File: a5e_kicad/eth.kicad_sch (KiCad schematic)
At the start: 54 parts, among them J9 RJ45_RB1-125B8G1A, U10 KSZ9031RNXCA, Y3 25MHz

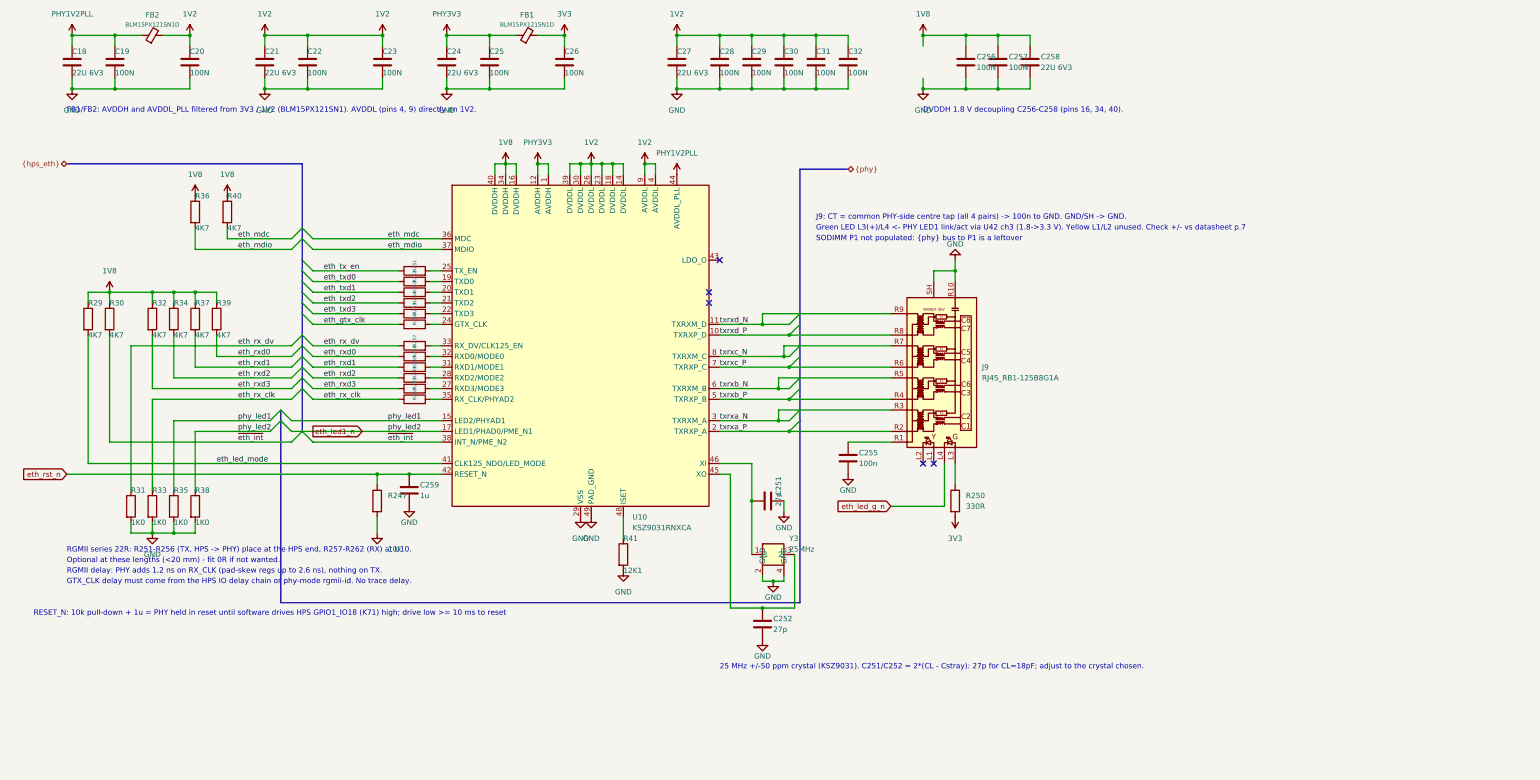
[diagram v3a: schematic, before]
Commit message: Ethernet PHY: KSZ9031RNX -> RTL8211FDI-CG (JLC stock, configured over MDIO)
The KSZ9031 had 16 orderable at JLC. The RTL8211FDI-CG (C692886) has 8.5k,
an internal 1.0 V LDO and only two straps.

- New symbol agilex_5_lib:RTL8211FDI-CG (QFN-40 5x5). Pins sit where the KSZ
  pins of the same function were, so the RGMII series resistors, MDI, crystal
  and RSET wiring are unchanged. The netlist was checked pin by pin.
- Straps: CFG_LDO = 10 (1.8 V I/O LDO) via R35 4K7 down on LED1 and new R268
  4K7 up on LED2. Everything else uses internal defaults (address 1). KSZ
  straps R29, R31-R34 and R37-R39 are DNP.
- Supplies: DVDD33 3V3, AVDD33 via FB1, LDO_OUT -> PHY1V0 (AVDD10/DVDD10,
  old 1V2 caps), DVDD_RG -> PHY_RG (caps only). FB2/C18/C19 DNP.
- PHYRSTB is a 3.3 V input: U42 ch3 now level-shifts eth_rst_n (1.8 V) to
  phy_rst_n. LED2 drives the J9 green LED directly.
- R36 MDIO pull-up 1K5, R41 RSET 2K49 1%.
- Notes on the sheet and ETH_PHY_REVIEW.md updated.
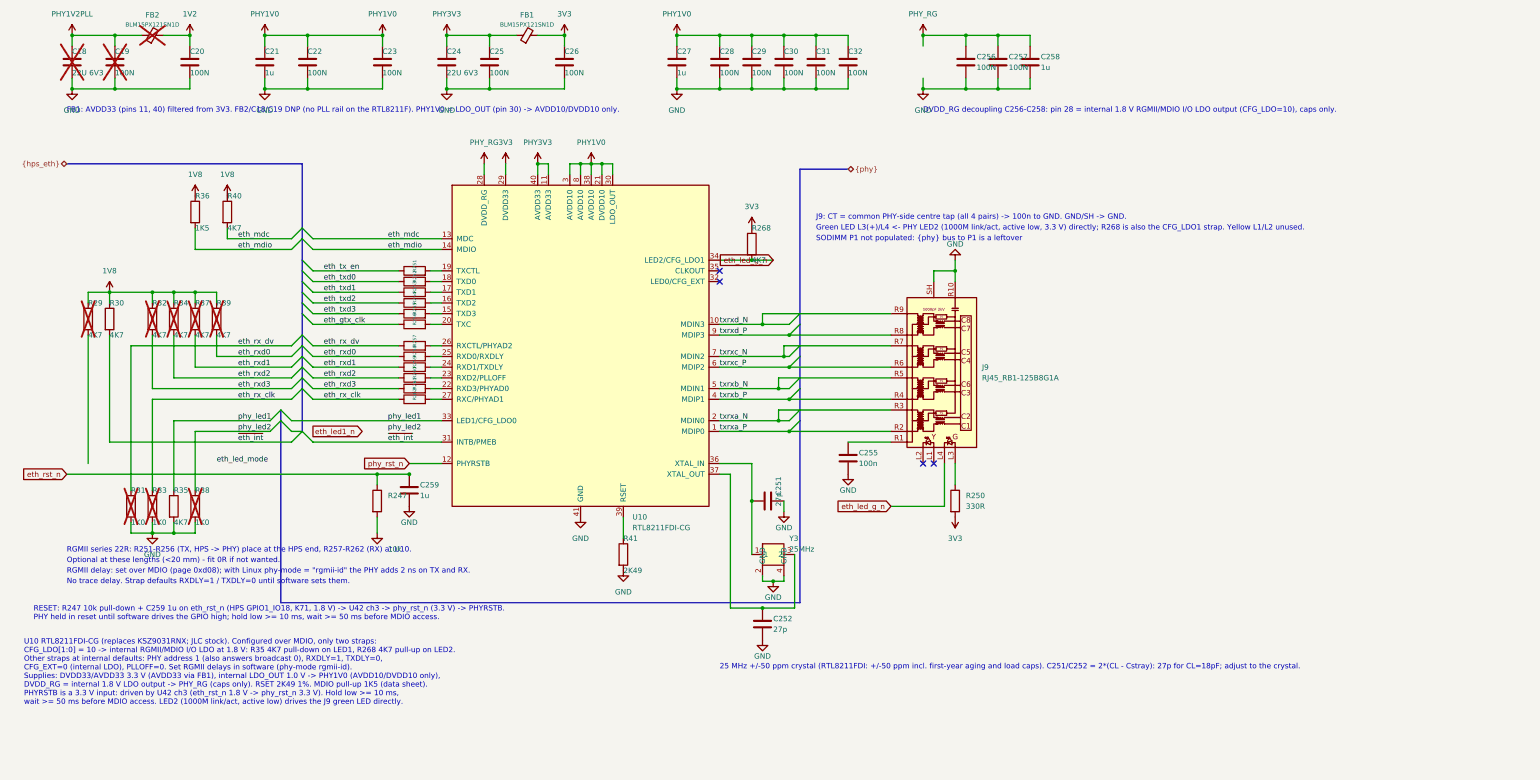
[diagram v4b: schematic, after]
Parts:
- added R268: 4K7, Resistor_SMD:R_0402_1005Metric, symbol Device:R
- C18, C19, FB2, R29, R31, R32, R33, R34, R37, R38, R39: now not fitted
- C21, C258, C27: value 22U 6V3 -> 1u; LCSC C415703 -> C52923
- R35: value 1K0 -> 4K7; LCSC C11702 -> C25900
- R36: value 4K7 -> 1K5; LCSC C25900 -> C25867
- R41: value 12K1 -> 2K49; LCSC C25852 -> C25884
- U10: value KSZ9031RNXCA -> RTL8211FDI-CG; footprint Package_DFN_QFN:QFN-48-1EP_7x7mm_P0.5mm_EP5.15x5.15mm -> Package_DFN_QFN:QFN-40-1EP_5x5mm_P0.4mm_EP3.6x3.6mm; symbol Interface_Ethernet:KSZ9031RNXCA -> agilex_5_lib:RTL8211FDI-CG; LCSC C58758 -> C692886
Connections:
- net 1V2: no longer C21.1, C22.1, C23.1, C27.1, C28.1, C29.1, C30.1, C31.1, C32.1, U10.14 (DVDDL), U10.18 (DVDDL), U10.23 (DVDDL), U10.26 (DVDDL), U10.30 (DVDDL), U10.39 (DVDDL), U10.4 (AVDDL), U10.9 (AVDDL)
- net 1V8: no longer C256.1, C257.1, C258.1, U10.16 (DVDDH), U10.34 (DVDDH), U10.40 (DVDDH)
- net 3V3: now also U10.29 (DVDD33), R268.1
- net GND: now also U10.41 (GND); no longer U10.29 (VSS), U10.49 (PAD_GND)
- net PHY1V2PLL: no longer U10.44 (AVDDL_PLL)
- net PHY3V3: now also U10.11 (AVDD33), U10.40 (AVDD33); no longer U10.1 (AVDDH), U10.12 (AVDDH)
- net eth_led1_n: no longer R38.1, U10.17 (LED1/PHAD0/PME_N1)
- net eth_led_g_n: now also U10.34 (LED2/CFG_LDO1), R268.2
- net eth_led_mode: no longer R29.2, U10.41 (CLK125_NDO/LED_MODE)
- net eth_mdc: now also U10.13 (MDC); no longer U10.36 (MDC)
- net eth_mdio: now also U10.14 (MDIO); no longer U10.37 (MDIO)
- net eth_rst_n: no longer U10.42 (RESET_N)
- net phy_led1: now also U10.33 (LED1/CFG_LDO0); no longer U10.15 (LED2/PHYAD1)
- net txrxa_N: now also U10.2 (MDIN0); no longer U10.3 (TXRXM_A)
- net txrxa_P: now also U10.1 (MDIP0); no longer U10.2 (TXRXP_A)
- net txrxb_N: now also U10.5 (MDIN1); no longer U10.6 (TXRXM_B)
- net txrxb_P: now also U10.4 (MDIP1); no longer U10.5 (TXRXP_B)
- net txrxc_N: now also U10.7 (MDIN2); no longer U10.8 (TXRXM_C)
- net txrxc_P: now also U10.6 (MDIP2); no longer U10.7 (TXRXP_C)
- net txrxd_N: now also U10.10 (MDIN3); no longer U10.11 (TXRXM_D)
- net txrxd_P: now also U10.9 (MDIP3); no longer U10.10 (TXRXP_D)
- net ~{eth_int}: now also U10.31 (INTB/PMEB); no longer U10.38 (INT_N/PME_N2)
- net at C252.1, Y3.3 (2): now also U10.37 (XTAL_OUT); no longer U10.45 (XO)
- net at R41.1: now also U10.39 (RSET); no longer U10.48 (ISET)
- net at R262.2: now also U10.27 (RXC/PHYAD1); no longer U10.35 (RX_CLK/PHYAD2)
- net at R256.2: now also U10.20 (TXC); no longer U10.24 (GTX_CLK)
- net at R252.2: now also U10.18 (TXD0); no longer U10.19 (TXD0)
- net at R253.2: now also U10.17 (TXD1); no longer U10.20 (TXD1)
- net at R254.2: now also U10.16 (TXD2); no longer U10.21 (TXD2)
- net at R255.2: now also U10.15 (TXD3); no longer U10.22 (TXD3)
- net at R251.2: now also U10.19 (TXCTL); no longer U10.25 (TX_EN)
- net at R261.2: now also U10.22 (RXD3/PHYAD0); no longer U10.27 (RXD3/MODE3)
- net at R260.2: now also U10.23 (RXD2/PLLOFF); no longer U10.28 (RXD2/MODE2)
- net at R259.2: now also U10.24 (RXD1/TXDLY); no longer U10.31 (RXD1/MODE1)
- net at R258.2: now also U10.25 (RXD0/RXDLY); no longer U10.32 (RXD0/MODE0)
- net at R257.2: now also U10.26 (RXCTL/PHYAD2); no longer U10.33 (RX_DV/CLK125_EN)
- net at C251.1, Y3.1: now also U10.36 (XTAL_IN); no longer U10.46 (XI)
- new net PHY1V0: C21.1, C22.1, C23.1, C27.1, C28.1, C29.1, C30.1, C31.1, C32.1, U10.21 (DVDD10), U10.3 (AVDD10), U10.30 (LDO_OUT), U10.38 (AVDD10), U10.8 (AVDD10)
- new net PHY_RG: C256.1, C257.1, C258.1, U10.28 (DVDD_RG)
- new net phy_led2: R38.1
- new net phy_rst_n: U10.12 (PHYRSTB)
- no-connect marks 5 -> 4
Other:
- note added: "25 MHz +/-50 ppm crystal (RTL8211FDI: +/-50 ppm incl. first-year aging and load caps). C251/C252 = 2*(CL - Cstray): 27p for CL=18pF; adjust to the crystal."
- note added: "DVDD_RG decoupling C256-C258: pin 28 = internal 1.8 V RGMII/MDIO I/O LDO output (CFG_LDO=10), caps only."
- note added: "FB1: AVDD33 (pins 11, 40) filtered from 3V3. FB2/C18/C19 DNP (no PLL rail on the RTL8211F). PHY1V0 = LDO_OUT (pin 30) -> AVDD10/DVDD10 only."
- note added: "Green LED L3(+)/L4 <- PHY LED2 (1000M link/act, active low, 3.3 V) directly; R268 is also the CFG_LDO1 strap. Yellow L1/L2 unused."
- note added: "No trace delay. Strap defaults RXDLY=1 / TXDLY=0 until software sets them."
- note added: "RESET: R247 10k pull-down + C259 1u on eth_rst_n (HPS GPIO1_IO18, K71, 1.8 V) -> U42 ch3 -> phy_rst_n (3.3 V) -> PHYRSTB. PHY held in reset until software drives the GPIO high; hold low >= 10 ms, wait >= 50 ms before MDIO access."
- note added: "RGMII delay: set over MDIO (page 0xd08); with Linux phy-mode = "rgmii-id" the PHY adds 2 ns on TX and RX."
- note added: "U10 RTL8211FDI-CG (replaces KSZ9031RNX; JLC stock). Configured over MDIO, only two straps: CFG_LDO[1:0] = 10 -> internal RGMII/MDIO I/O LDO at 1.8 V: R35 4K7 pull-down on LED1, R268 4K7 pull-up on LED2. Other straps at internal defaults: PHY address 1 (also answers broadcast 0), RXDLY=1, TXDLY=0, CFG_EXT=0 (internal LDO), PLLOFF=0. Set RGMII delays in software (phy-mode rgmii-id). Supplies: DVDD3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"
- note removed: "25 MHz +/-50 ppm crystal (KSZ9031). C251/C252 = 2*(CL - Cstray): 27p for CL=18pF; adjust to the crystal chosen."
- note removed: "DVDDH 1.8 V decoupling C256-C258 (pins 16, 34, 40)."
- note removed: "FB1/FB2: AVDDH and AVDDL_PLL filtered from 3V3 / 1V2 (BLM15PX121SN1). AVDDL (pins 4, 9) directly on 1V2."
- note removed: "GTX_CLK delay must come from the HPS IO delay chain or phy-mode rgmii-id. No trace delay."
- note removed: "Green LED L3(+)/L4 <- PHY LED1 link/act via U42 ch3 (1.8->3.3 V). Yellow L1/L2 unused. Check +/- vs datasheet p.7"
- note removed: "RESET_N: 10k pull-down + 1u = PHY held in reset until software drives HPS GPIO1_IO18 (K71) high; drive low >= 10 ms to reset"
- note removed: "RGMII delay: PHY adds 1.2 ns on RX_CLK (pad-skew regs up to 2.6 ns), nothing on TX."

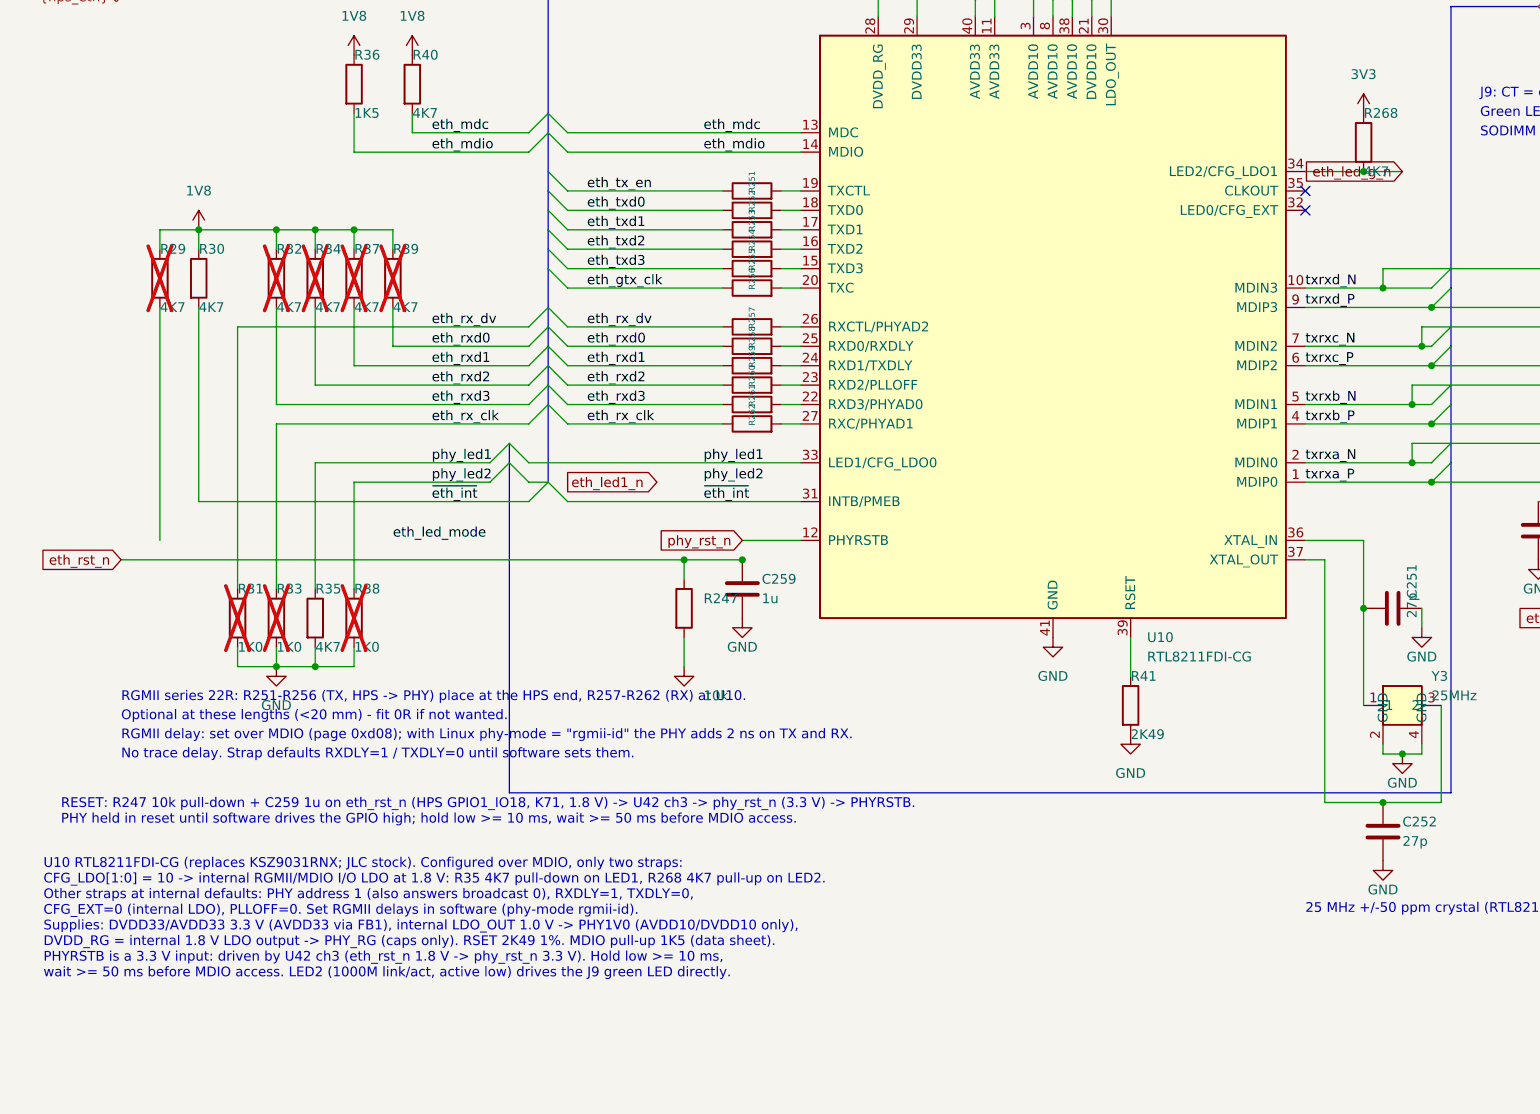
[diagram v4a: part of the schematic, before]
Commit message: Ethernet PHY: fit all nine RTL8211F config straps (data sheet 7.8)
The data sheet requires an external pull on every CONFIG pin, so the
internal pulls aren't enough (pointed out by the Ti135 session). 4K7 each:
- PHYAD=001: R32 up, R33 and R31 down (R31/R33 1K0 -> 4K7, re-fitted).
- PLLOFF=0: new R269 down. TXDLY=0: new R270 down. RXDLY=1: R39 up.
- CFG_EXT=0: new R271 down. CFG_LDO=10: R35 down, R268 up.
RX straps and INTB pull up to PHY_RG (DVDD_RG), not the board 1V8. R34/R37
stay DNP (wrong direction). Notes added: 3V3 rise time >= 0.5 ms and LED2
LCR setting.
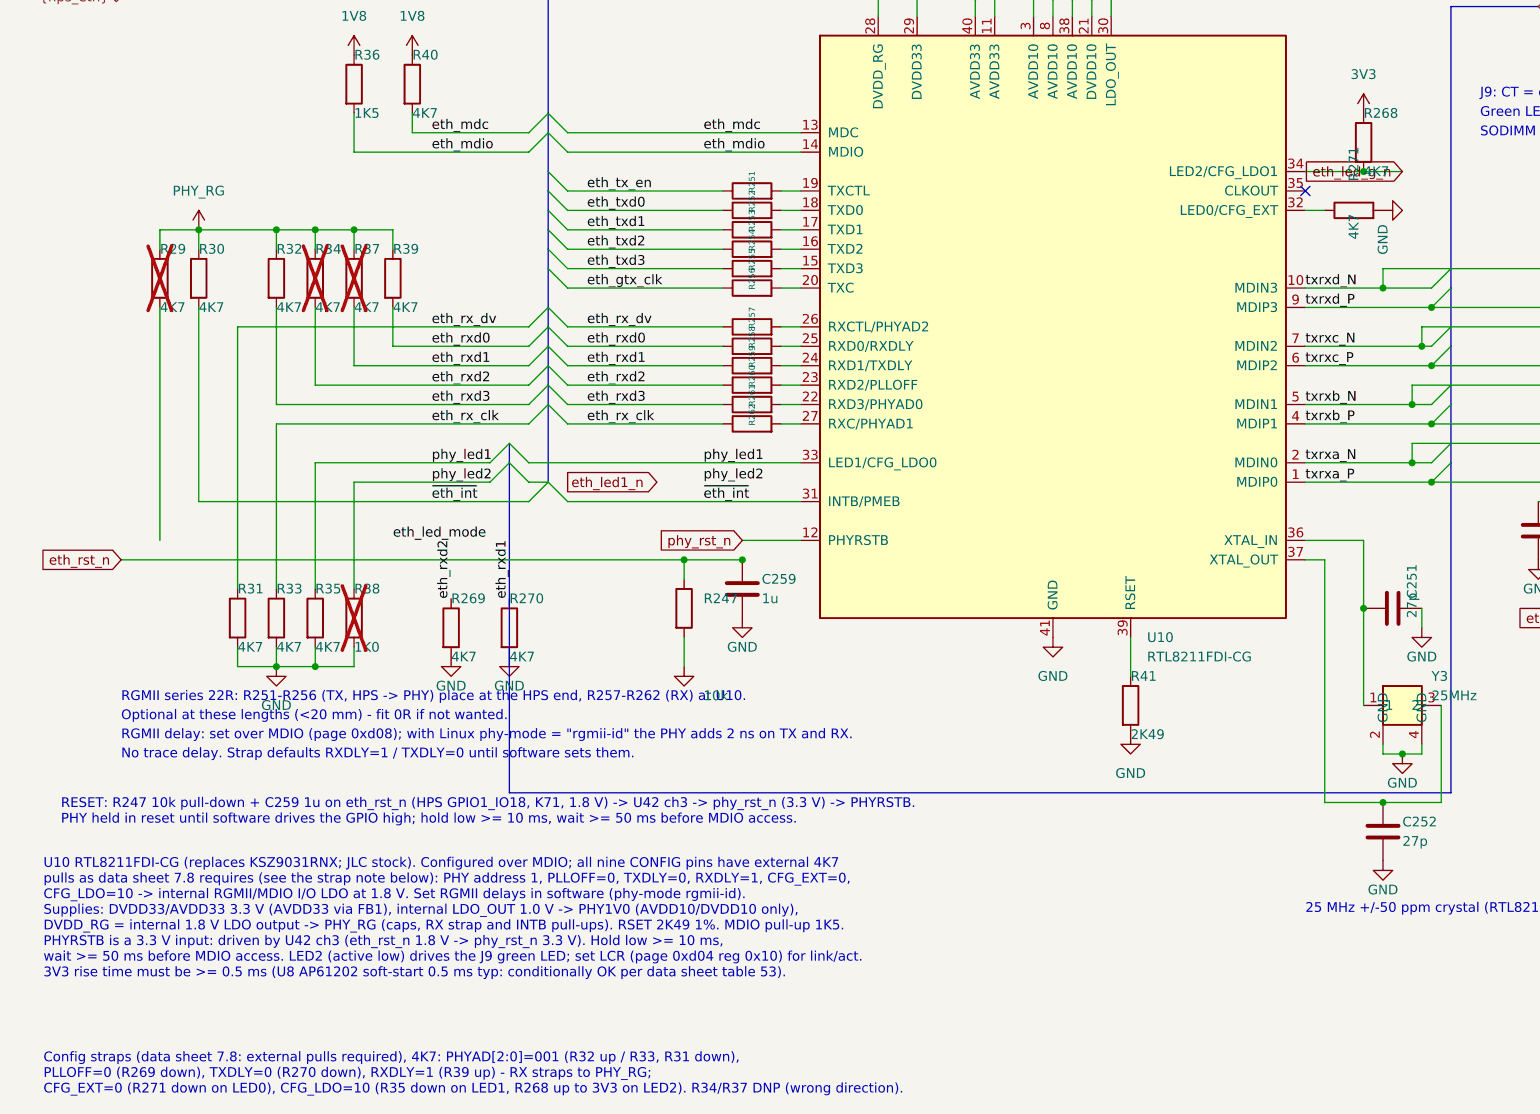
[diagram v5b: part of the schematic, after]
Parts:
- added R269, R270, R271: 4K7, Resistor_SMD:R_0402_1005Metric, symbol Device:R
- R31, R33: value 1K0 -> 4K7; LCSC C11702 -> C25900; now fitted
- R32, R39: now fitted
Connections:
- net 1V8: no longer R29.1, R30.1, R32.1, R34.1, R37.1, R39.1
- net GND: now also R269.2, R270.2, R271.2
- net PHY_RG: now also R29.1, R30.1, R32.1, R34.1, R37.1, R39.1
- net eth_rxd1: now also R270.1
- net eth_rxd2: now also R269.1
- net at U10.32 (LED0/CFG_EXT): now also R271.1
- no-connect marks 4 -> 3
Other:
- note added: "Config straps (data sheet 7.8: external pulls required), 4K7: PHYAD[2:0]=001 (R32 up / R33, R31 down), PLLOFF=0 (R269 down), TXDLY=0 (R270 down), RXDLY=1 (R39 up) - RX straps to PHY_RG; CFG_EXT=0 (R271 down on LED0), CFG_LDO=10 (R35 down on LED1, R268 up to 3V3 on LED2). R34/R37 DNP (wrong direction)."
- note added: "U10 RTL8211FDI-CG (replaces KSZ9031RNX; JLC stock). Configured over MDIO; all nine CONFIG pins have external 4K7 pulls as data sheet 7.8 requires (see the strap note below): PHY address 1, PLLOFF=0, TXDLY=0, RXDLY=1, CFG_EXT=0, CFG_LDO=10 -> internal RGMII/MDIO I/O LDO at 1.8 V. Set RGMII delays in software (phy-mode rgmii-id). Supplies: DVDD33/AVDD33 3.3 V (AVDD33 via FB1), internal LDO_OUT 1.0 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"
- note removed: "U10 RTL8211FDI-CG (replaces KSZ9031RNX; JLC stock). Configured over MDIO, only two straps: CFG_LDO[1:0] = 10 -> internal RGMII/MDIO I/O LDO at 1.8 V: R35 4K7 pull-down on LED1, R268 4K7 pull-up on LED2. Other straps at internal defaults: PHY address 1 (also answers broadcast 0), RXDLY=1, TXDLY=0, CFG_EXT=0 (internal LDO), PLLOFF=0. Set RGMII delays in software (phy-mode rgmii-id). Supplies: DVDD3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"

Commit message: Schematic reorg step 1: remove dangling stubs and stale notes, correct notes, fill title blocks
Netlist: 0 renamed, 0 connectivity diffs; DRC parity 0. ERC 315 -> 242.
Plan refreshed for the eMMC, RTL8211FDI, TPS548A28 and the tuned LPDDR4 (IOBANK 3 sheet name kept).
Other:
- title: (none) -> Ethernet: RTL8211FDI PHY and RJ45
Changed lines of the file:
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@@
 	(paper "A4")
 	(title_block
-		(rev "0.1")
+		(title "Ethernet: RTL8211FDI PHY and RJ45")
+		(rev "${REVISION}")
+		(comment 1 "${BOARD}")
 	)
 	(text "25 MHz +/-50 ppm crystal (RTL8211FDI: +/-50 ppm incl. first-year aging and load caps). C251/C252 = 2*(CL - Cstray): 27p for CL=18pF; adjust to the crystal."
